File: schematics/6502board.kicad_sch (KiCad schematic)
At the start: 35 parts, among them J1 Power, J2 DEBUG, J3 I2C, J4 Serial, J5 Spare CS, SW1 Reset, U1 W65C02S6TQG, U10 TL16C750E, U2 IS61LV256AL, U3 74LVC139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

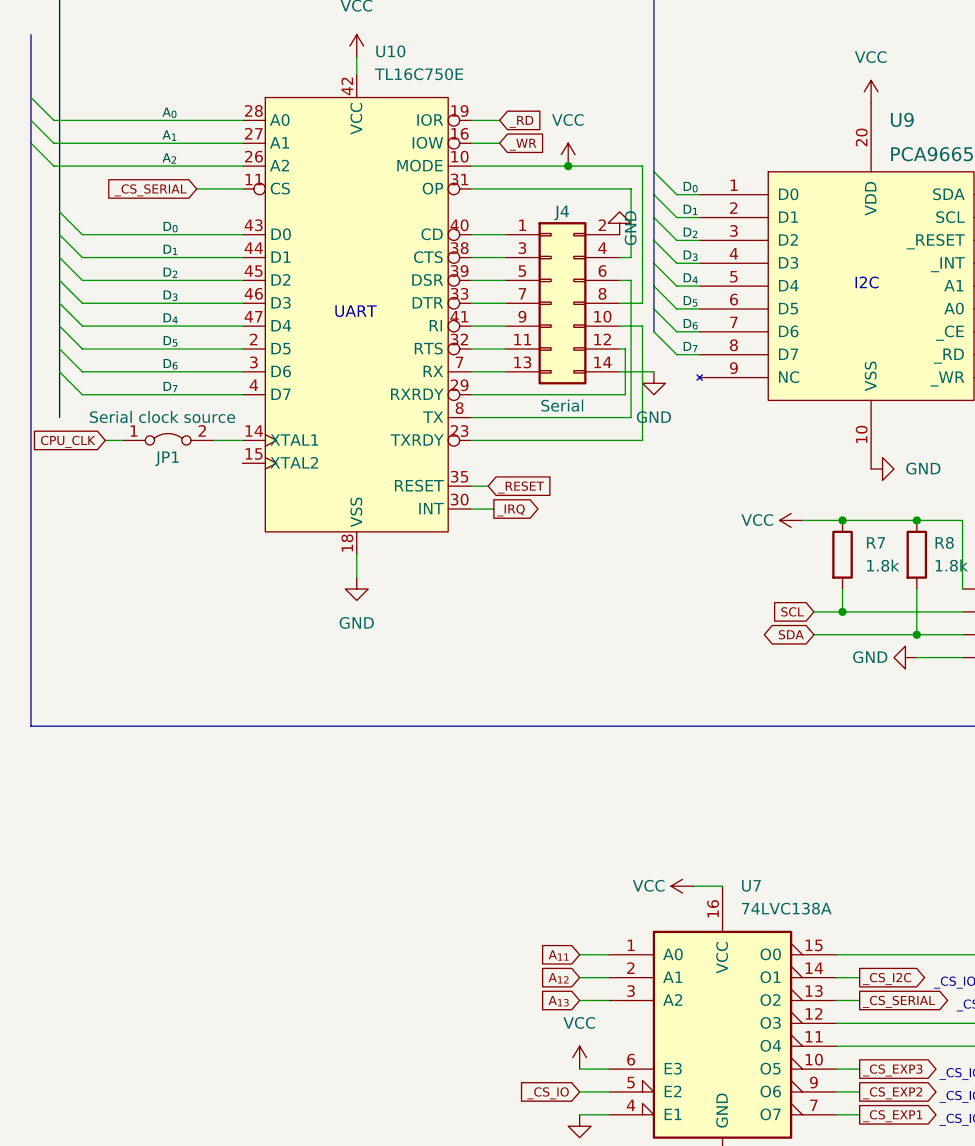
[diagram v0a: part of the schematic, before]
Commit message: Invert IRQ and RESET for UART. Experiment with vias.
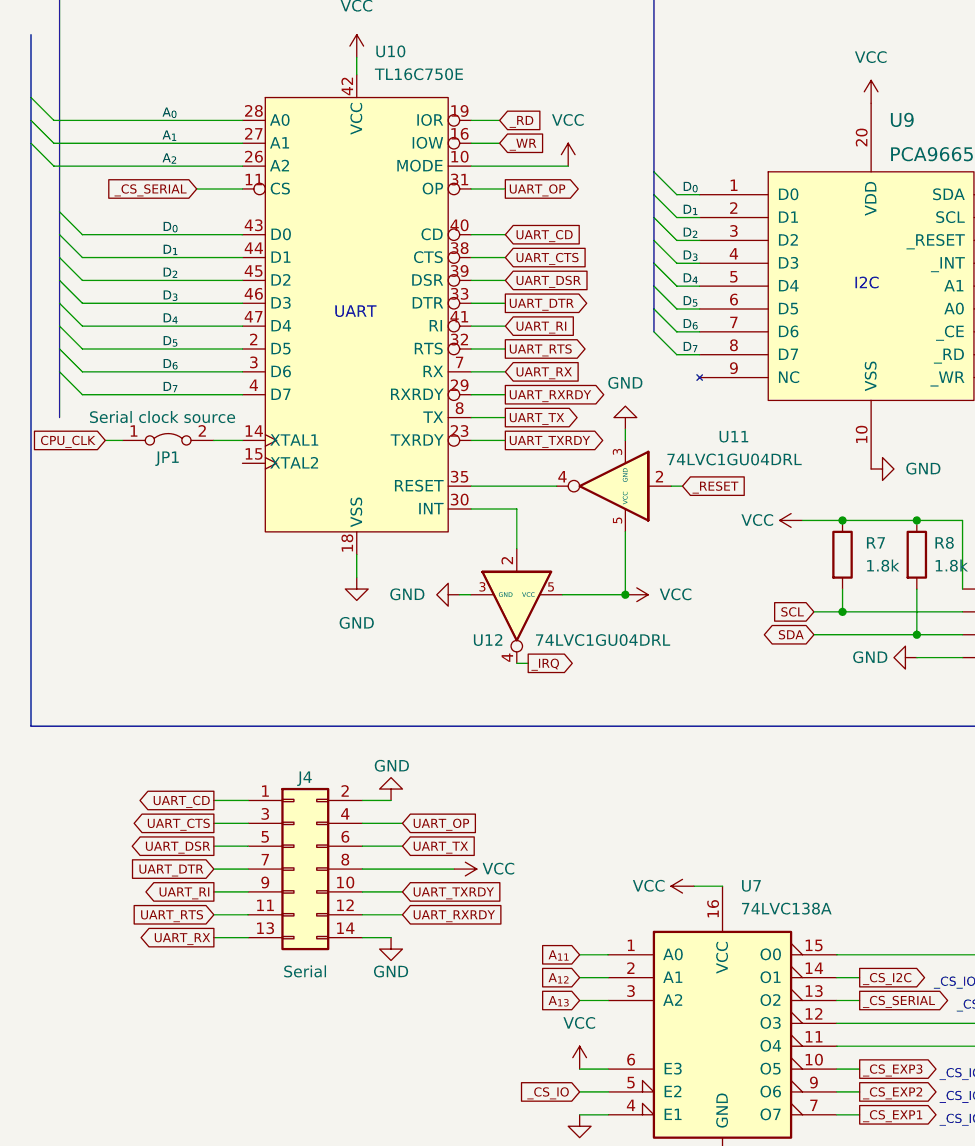
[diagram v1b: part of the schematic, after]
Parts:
- added U11, U12: 74LVC1GU04DRL, Package_TO_SOT_SMD:SOT-553, symbol 74xGxx:74LVC1GU04DRL
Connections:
- net GND: now also U11.3 (GND), U12.3 (GND)
- net VCC: now also U11.5 (VCC), U12.5 (VCC)
- net _IRQ: now also U12.4; no longer U10.30 (INT)
- net _RESET: now also U11.2; no longer U10.35 (RESET)
- net UART_TXRDY: now reaches J4.10 (Pin_10), U10.23 (TXRDY)
- net UART_RXRDY: now reaches J4.12 (Pin_12), U10.29 (RXRDY)
- net UART_OP: now reaches J4.4 (Pin_4), U10.31 (OP)
- net UART_RTS: now reaches J4.11 (Pin_11), U10.32 (RTS)
- net UART_DTR: now reaches J4.7 (Pin_7), U10.33 (DTR)
- net UART_CTS: now reaches J4.3 (Pin_3), U10.38 (CTS)
- net UART_DSR: now reaches J4.5 (Pin_5), U10.39 (DSR)
- net UART_CD: now reaches J4.1 (Pin_1), U10.40 (CD)
- net UART_RI: now reaches J4.9 (Pin_9), U10.41 (RI)
- net UART_RX: now reaches J4.13 (Pin_13), U10.7 (RX)
- net UART_TX: now reaches J4.6 (Pin_6), U10.8 (TX)
- new net: U10.30 (INT), U12.2
- new net: U10.35 (RESET), U11.4
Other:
- moved on the sheet: J4
